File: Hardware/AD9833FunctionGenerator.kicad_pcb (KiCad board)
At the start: 2 copper layers, 124.5 x 114.3 mm, 52 parts, among them U1 LM7805_TO220

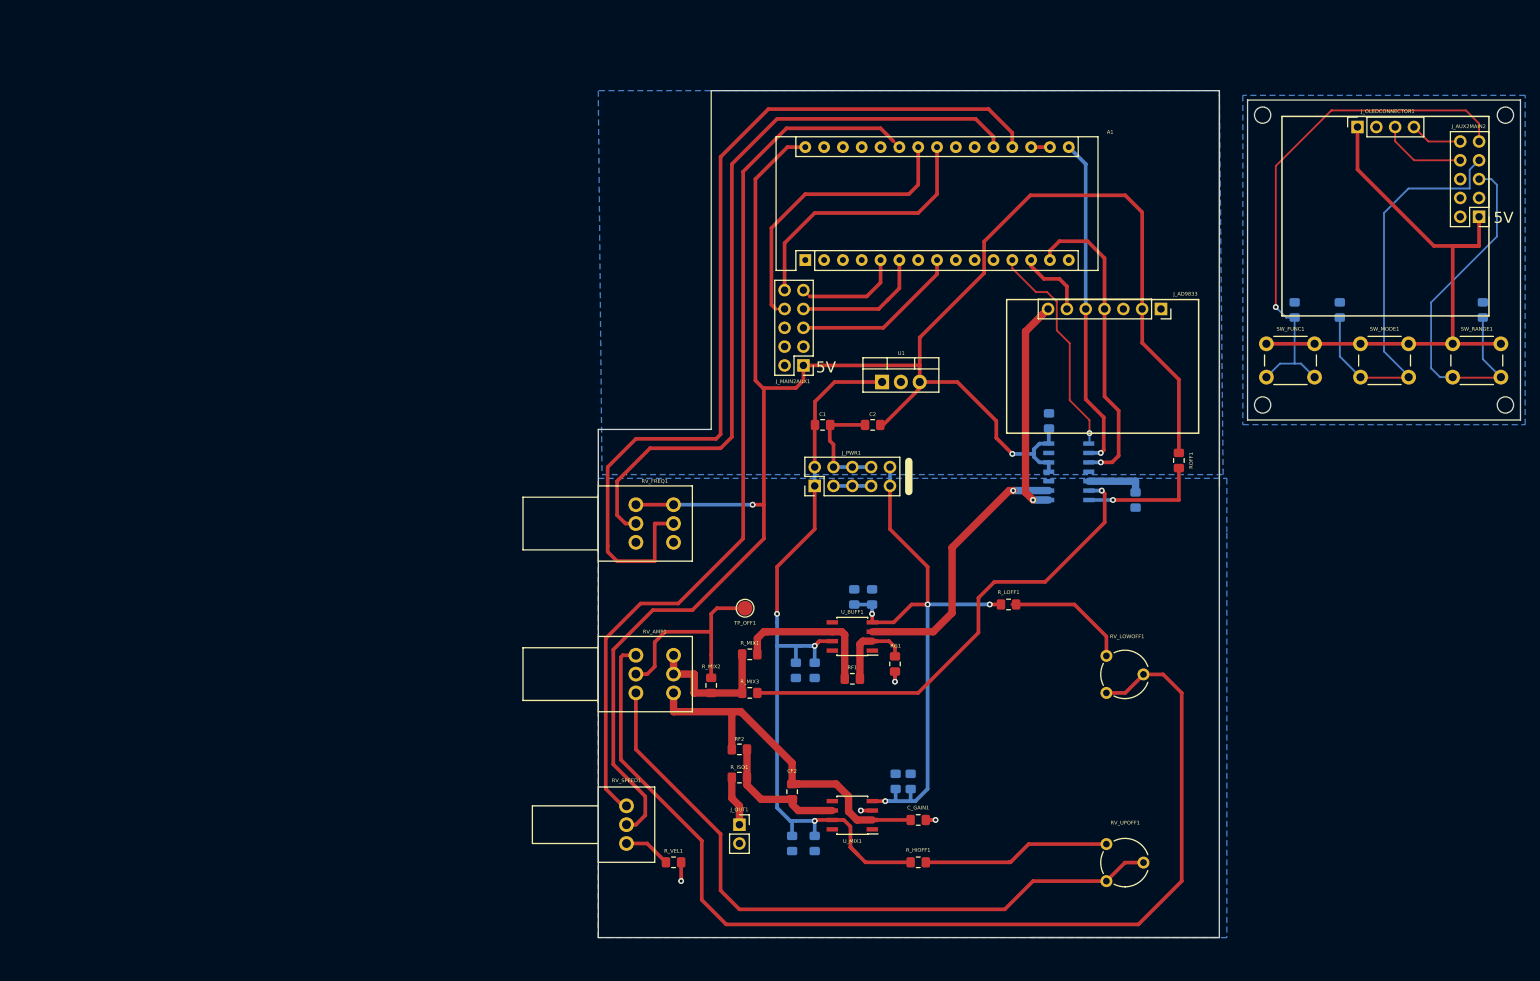
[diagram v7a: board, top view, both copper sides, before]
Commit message: Removed power traces from ground plane. improved horizontal component distribution. added right-angle PCB mount DPDT power switch.
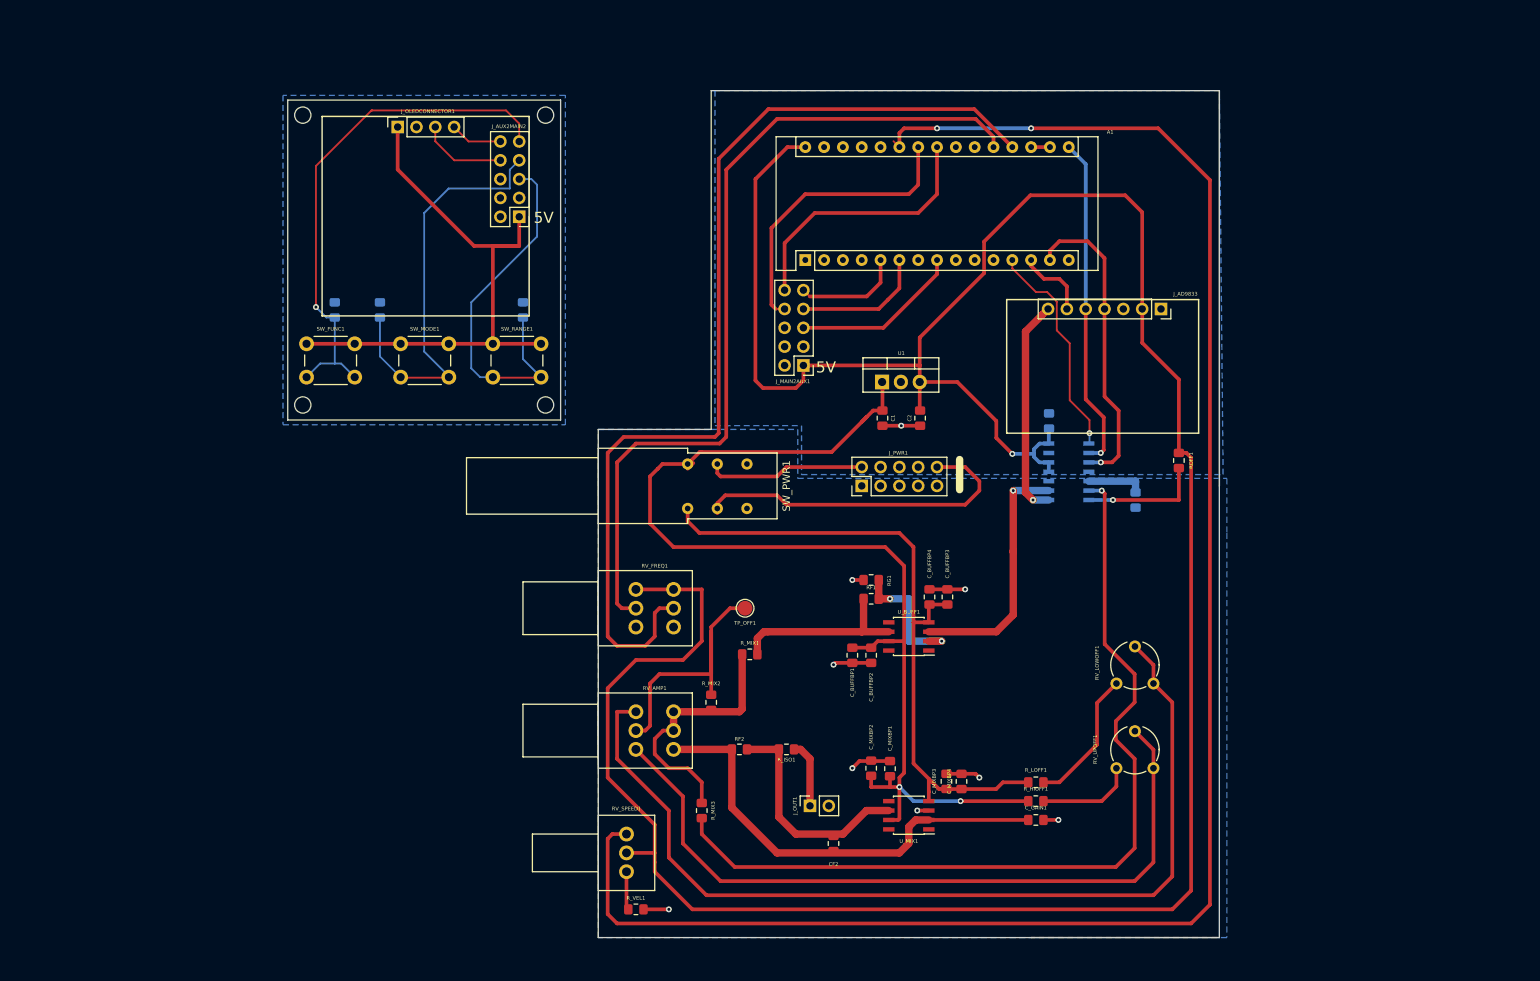
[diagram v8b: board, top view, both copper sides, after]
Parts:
- added SW_PWR1: SW_DPDT_x2, ALPS_SPUN191600:ALPS_SPUN191600, F.Cu at (131.4, 88.9)
- C1: value 330nF -> 220nF
- C_BUFFBP1, C_BUFFBP2, C_BUFFBP3, C_BUFFBP4, C_MIXBP1, C_MIXBP2, C_MIXBP3, C_MIXBP4: moved to F.Cu
- moved J_AUX2MAIN2 129.5 mm to (108.7, 52.6)
- moved J_OLEDCONNECTOR1 129.5 mm to (92.3, 40.5)
- moved REF** 129.5 mm to (79.5, 78.0)
- moved REF** 129.5 mm to (79.5, 38.9)
- moved R_FUNC1 129.5 mm to (83.8, 65.2)
- moved SW_FUNC1 129.5 mm to (80.0, 69.7)
- moved SW_MODE1 129.5 mm to (92.7, 69.7)
- moved REF** 129.5 mm to (112.3, 78.0)
- moved REF** 129.5 mm to (112.3, 38.9)
- moved R_MODE1 129.5 mm to (89.9, 65.2)
- moved R_RANGE1 129.5 mm to (109.2, 65.2)
- moved SW_RANGE1 129.5 mm to (105.2, 69.7)
- moved R_LOFF1 24.3 mm to (178.4, 128.9)
- moved R_HIOFF1 17.9 mm to (178.4, 131.4)
- moved R_MIX3 17.1 mm to (133.3, 132.7), turned to 90 degrees
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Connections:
- J_PWR1 pad 1: /+12V -> (no net)
- J_PWR1 pad 10: /-12V -> Net-(J_PWR1-Pad10)
- J_PWR1 pad 2: /+12V -> Net-(J_PWR1-Pad2)
- J_PWR1 pad 9: /-12V -> (no net)
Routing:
- net /VEL1: track 122.5 -> 241.7 mm, vias 0 -> 2
- net /5V: track 272.4 -> 375.8 mm, vias 2 -> 1
- net /OFFSETADJUST: track 65.0 -> 117.4 mm
- net Net-(J_PWR1-Pad10): track 0.00 -> 46.2 mm
- net /+12V: track 107.5 -> 152.1 mm, vias 3 -> 2
- net Net-(J_PWR1-Pad2): track 0.00 -> 21.4 mm
- net /AGND: track 11.9 -> 28.5 mm, vias 4 -> 8
- net Net-(RV_AMP1-Pad3): track 145.7 -> 129.3 mm
- net Net-(RV_AMP1-Pad5): track 19.4 -> 35.1 mm
- net /FREQ2: track 102.6 -> 115.4 mm
- net Net-(CF2-Pad1): track 18.2 -> 30.5 mm
- net Net-(CF2-Pad2): track 49.3 -> 61.7 mm
- net Net-(RV_UPOFF1-Pad3): track 25.4 -> 13.1 mm
- net /GND: track 15.7 -> 5.08 mm, vias 0 -> 1
- net /FREQ1: track 125.7 -> 135.8 mm
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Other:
- board size 124.5 x 114.3 mm -> 125.7 x 114.3 mm
